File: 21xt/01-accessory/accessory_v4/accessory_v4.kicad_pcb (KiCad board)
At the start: 4 copper layers, 64.5 x 80.8 mm, 143 parts, among them IC1 LT6658AHMSE-2.5#PBF, IC10 TPS2113ADRBR, IC2 LT6658AHMSE-5#PBF, IC3 REF3450IDBVR, IC4 INA827AIDGK, IC5 INA827AIDGK, IC6 TXB0108PWR, IC7 AD8591ARTZ-REEL7, IC8 AD5689RARUZ-RL7, IC9 AD7175-8BCPZ-RL7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

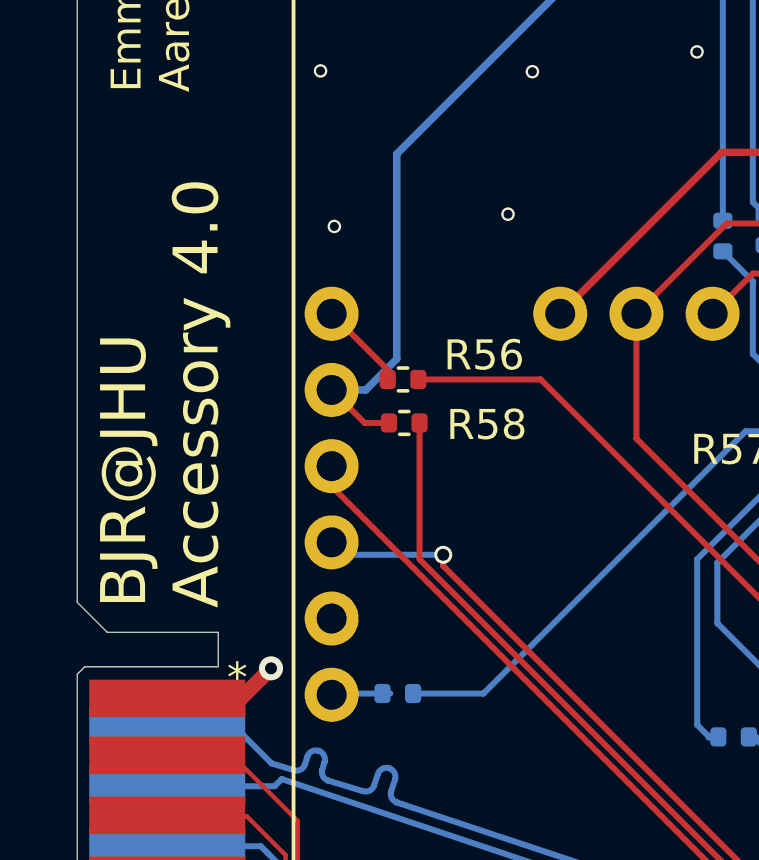
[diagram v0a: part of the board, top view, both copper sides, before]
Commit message: Finished accessory & peripheral layout revisions
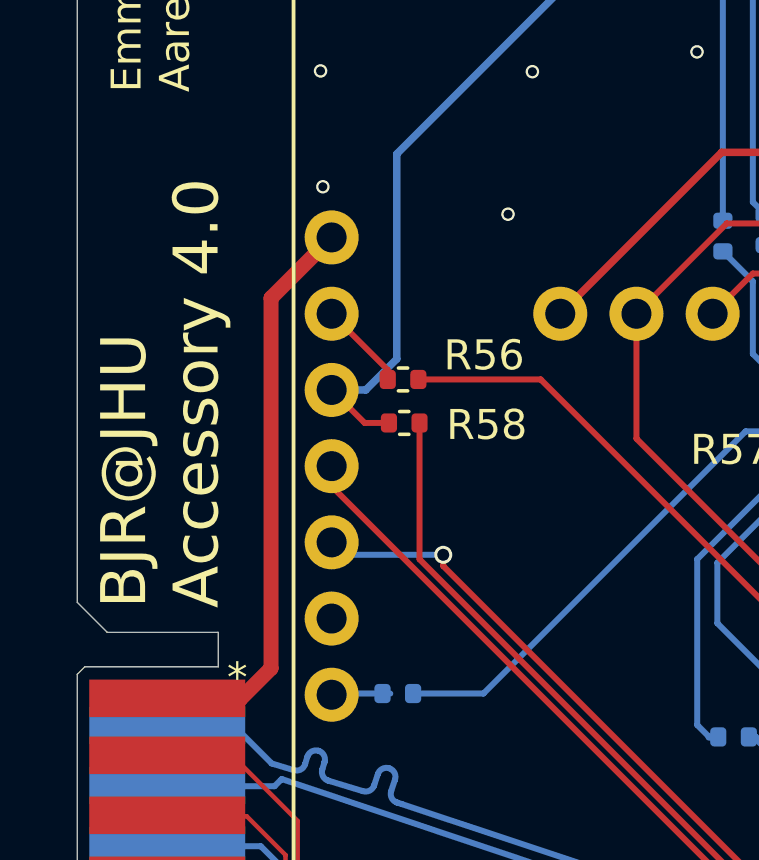
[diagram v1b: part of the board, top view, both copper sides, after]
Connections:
- J2 pad 1: usb_gnd -> LED_control
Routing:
- net LED_control: track 0.00 -> 19.1 mm
- net usb_gnd: track 226.4 -> 222.5 mm, vias 143 -> 142
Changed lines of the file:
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@@
 	(net 144 "3v3_pre")
 	(net 145 "3v3_pre2")
+	(net 146 "LED_control")
 	(footprint "Capacitor_SMD:C_0402_1005Metric"
 		(layer "F.Cu")
@@
 			(size 5.2 1.25)
 			(layers "F.Cu" "F.Mask")
-			(net 140 "usb_gnd")
+			(net 146 "LED_control")
 			(pinfunction "Pin_1")
 			(pintype "passive")
@@
 			(solder_mask_margin 0.102)
 		)
+		(pad "37" thru_hole circle
+			(at 21.844 -7.62 90)
+			(size 1.8 1.8)
+			(drill 1)
+			(layers "*.Cu" "*.Mask")
+			(remove_unused_layers no)
+			(net 146 "LED_control")
+			(pinfunction "CS3")
+			(pintype "bidirectional")
+			(solder_mask_margin 0.102)
+		)
 		(pad "38" thru_hole circle
 			(at 19.3 -7.62 90)
@@
 	)
 	(segment
-		(start 3.4798 35.9294)
-		(end 5.9298 35.9294)
-		(width 0.5)
-		(layer "F.Cu")
-		(net 140)
-	)
-	(segment
 		(start 46.54 60.96)
 		(end 47.44 60.96)
@@
 	)
 	(segment
-		(start 5.9298 35.9294)
-		(end 6.9596 34.8996)
-		(width 0.5)
-		(layer "F.Cu")
-		(net 140)
-	)
-	(segment
 		(start 26.7 12.7)
 		(end 26.7 15.95)
@@
 	)
 	(via
+		(at 8.6868 18.8468)
+		(size 0.45)
+		(drill 0.3)
+		(layers "F.Cu" "B.Cu")
+		(free yes)
+		(net 140)
+	)
+	(via
 		(at 29.89 55.17)
 		(size 0.6)
@@
 	)
 	(via
-		(at 9.07 20.17)
-		(size 0.45)
-		(drill 0.3)
-		(layers "F.Cu" "B.Cu")
-		(free yes)
-		(net 140)
-	)
-	(via
 		(at 33.3 13.84)
 		(size 0.45)
@@
 	)
 	(via
-		(at 6.9596 34.8996)
-		(size 0.8)
-		(drill 0.4)
-		(layers "F.Cu" "B.Cu")
-		(net 140)
-	)
-	(via
 		(at 37.8 8.035)
 		(size 0.45)
@@
 		(net 145)
 	)
+	(segment
+		(start 3.4798 35.9294)
+		(end 5.9298 35.9294)
+		(width 0.5)
+		(layer "F.Cu")
+		(net 146)
+	)
+	(segment
+		(start 6.9596 22.5564)
+		(end 8.98 20.536)
+		(width 0.5)
+		(layer "F.Cu")
+		(net 146)
+	)
+	(segment
+		(start 5.9298 35.9294)
+		(end 6.9596 34.8996)
+		(width 0.5)
+		(layer "F.Cu")
+		(net 146)
+	)
+	(segment
+		(start 6.9596 34.8996)
+		(end 6.9596 22.5564)
+		(width 0.5)
+		(layer "F.Cu")
+		(net 146)
+	)
 	(zone

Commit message: finished accessory v4
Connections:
- J2 pad 1: LED_control -> usb_gnd
- J2 pad 10: usb_gnd -> LED_control
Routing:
- net LED_control: track 19.1 -> 6.05 mm, vias 0 -> 1
- net usb_gnd: track 222.5 -> 220.7 mm
- net 5v_usb: track 49.9 -> 48.2 mm
- net usb_d+: track 40.5 -> 39.2 mm
- net usb_d-: track 37.7 -> 36.8 mm
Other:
- board text added: "LED"
